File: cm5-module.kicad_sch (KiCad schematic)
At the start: 0 parts

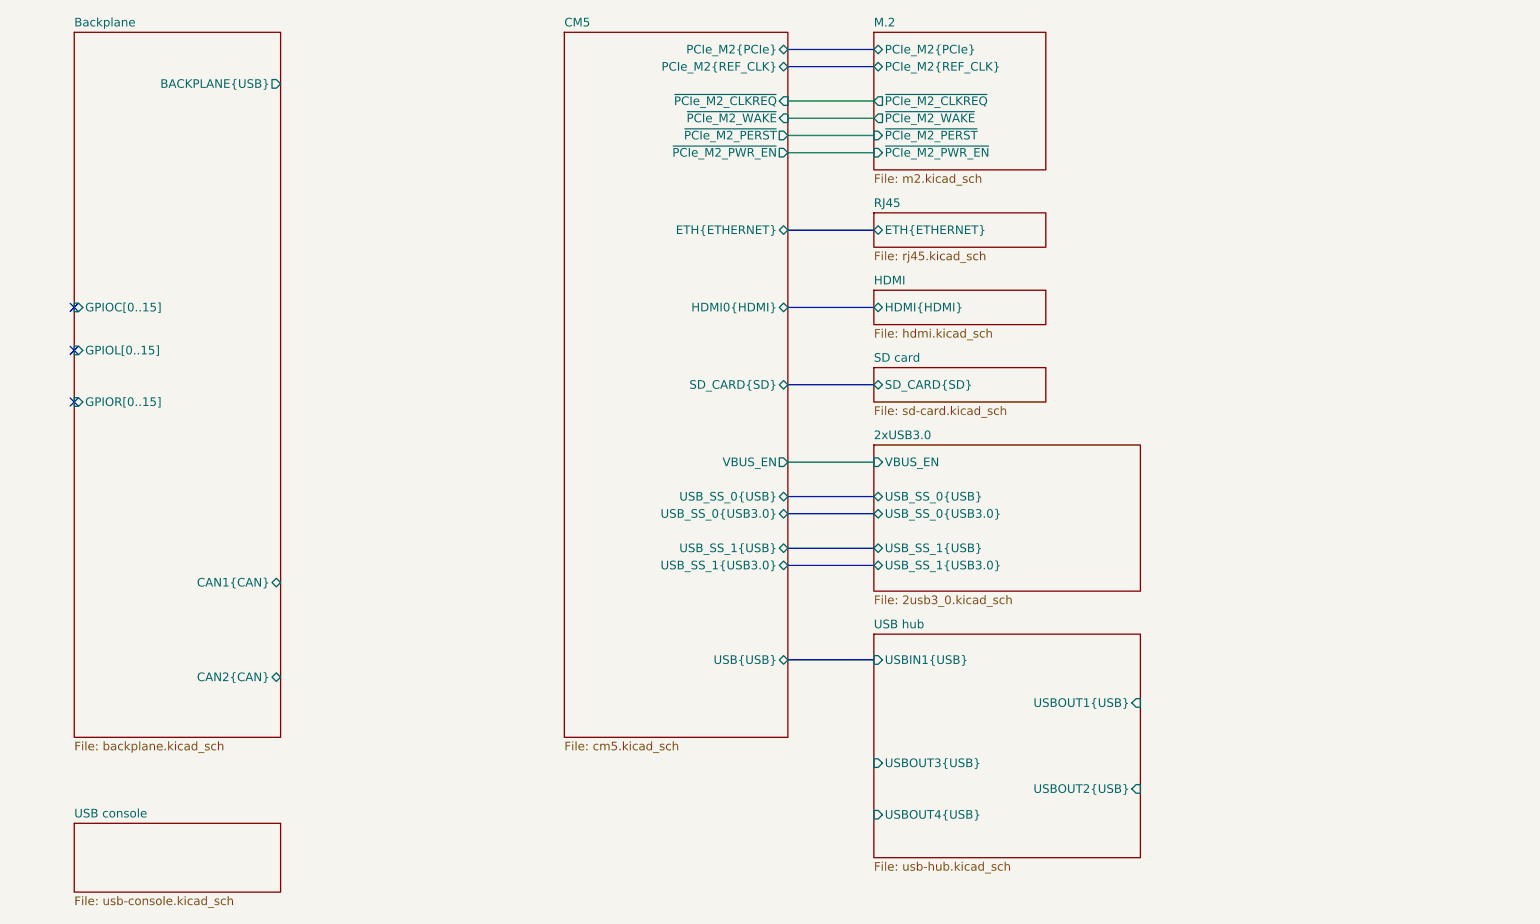
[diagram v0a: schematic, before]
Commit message: [#1] WIP: Change components to ones from the global library, refactor schematic
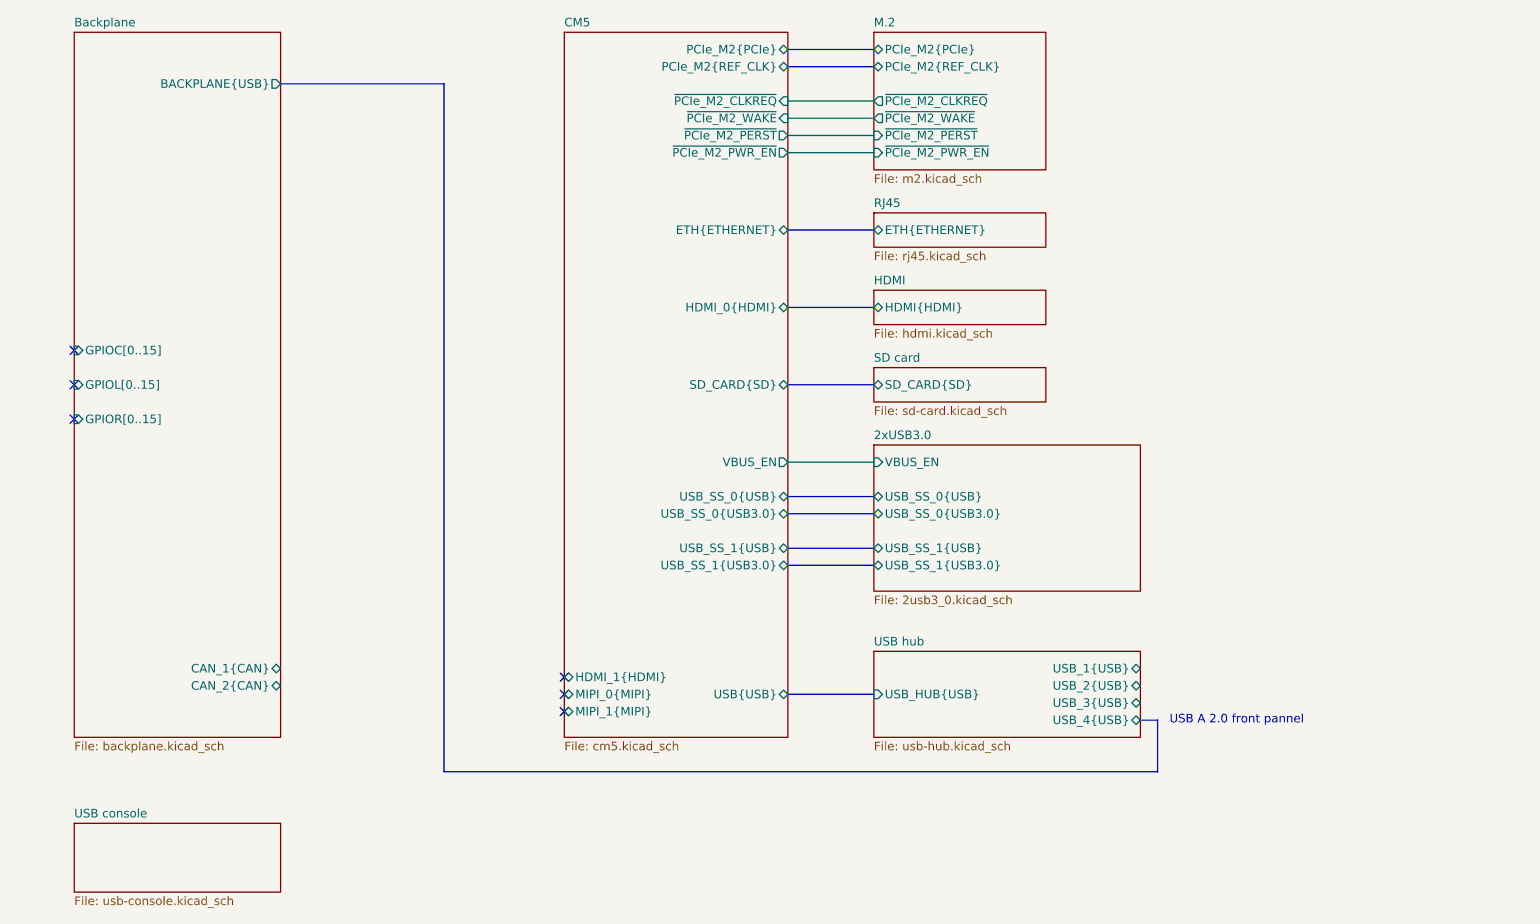
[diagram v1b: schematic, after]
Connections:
- no-connect marks 3 -> 6
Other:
- sheet Backplane ports: added CAN_1{CAN}, CAN_2{CAN}; removed CAN1{CAN}, CAN2{CAN}
- sheet CM5 ports: added HDMI_0{HDMI}, HDMI_1{HDMI}, MIPI_0{MIPI}, MIPI_1{MIPI}; removed HDMI0{HDMI}
- sheet USB hub ports: added USB_1{USB}, USB_2{USB}, USB_3{USB}, USB_4{USB}, USB_HUB{USB}; removed USBIN1{USB}, USBOUT1{USB}, USBOUT2{USB}, USBOUT3{USB}, USBOUT4{USB}
- note added: "USB A 2.0 front pannel"
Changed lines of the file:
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@@
 		(members "+" "-")
 	)
-	(no_connect
-		(at 46.99 78.74)
+	(text "USB A 2.0 front pannel"
+		(exclude_from_sim no)
+		(at 218.694 139.7 0)
+		(effects
+			(font
+				(size 1.27 1.27)
+			)
+		)
 	)
 	(no_connect
@@
 	)
 	(no_connect
-		(at 46.99 92.71)
+		(at 46.99 90.17)
+	)
+	(no_connect
+		(at 119.38 135.89)
+	)
+	(no_connect
+		(at 119.38 133.35)
+	)
+	(no_connect
+		(at 119.38 138.43)
+	)
+	(no_connect
+		(at 46.99 95.25)
 	)
 	(bus
@@
 	(bus
 		(pts
-			(xy 152.4 130.81) (xy 165.1 130.81)
+			(xy 152.4 135.89) (xy 165.1 135.89)
 		)
 		(stroke
@@
 	(bus
 		(pts
+			(xy 207.01 147.32) (xy 101.6 147.32)
+		)
+		(stroke
+			(width 0)
+			(type default)
+		)
+	)
+	(bus
+		(pts
+			(xy 101.6 147.32) (xy 101.6 45.72)
+		)
+		(stroke
+			(width 0)
+			(type default)
+		)
+	)
+	(bus
+		(pts
 			(xy 152.4 114.3) (xy 165.1 114.3)
 		)
@@
 		)
 	)
+	(bus
+		(pts
+			(xy 207.01 139.7) (xy 207.01 147.32)
+		)
+		(stroke
+			(width 0)
+			(type default)
+		)
+	)
 	(wire
 		(pts
@@
 		(pts
 			(xy 152.4 78.74) (xy 165.1 78.74)
+		)
+		(stroke
+			(width 0)
+			(type default)
+		)
+	)
+	(bus
+		(pts
+			(xy 204.47 139.7) (xy 207.01 139.7)
+		)
+		(stroke
+			(width 0)
+			(type default)
+		)
+	)
+	(bus
+		(pts
+			(xy 101.6 45.72) (xy 77.47 45.72)
 		)
 		(stroke
@@
 		)
 		(fill
-			(color 0 0 0 0.0000)
+			(color 255 255 194 1.0000)
 		)
 		(property "Sheetname" "USB console"
@@
 		)
 		(fill
-			(color 0 0 0 0.0000)
+			(color 255 255 194 1.0000)
 		)
 		(property "Sheetname" "M.2"
@@
 	)
 	(sheet
-		(at 165.1 127)
-		(size 39.37 33.02)
+		(at 165.1 129.54)
+		(size 39.37 12.7)
 		(exclude_from_sim no)
 		(in_bom yes)
@@
 		)
 		(fill
-			(color 0 0 0 0.0000)
+			(color 255 255 194 1.0000)
 		)
 		(property "Sheetname" "USB hub"
-			(at 165.1 126.2884 0)
+			(at 165.1 128.8284 0)
 			(effects
 				(font
@@
 		)
 		(property "Sheetfile" "usb-hub.kicad_sch"
-			(at 165.1 160.6046 0)
+			(at 165.1 142.8246 0)
 			(effects
 				(font
@@
 			)
 		)
-		(pin "USBIN1{USB}" input
-			(at 165.1 130.81 180)
-			(effects
-				(font
-					(size 1.27 1.27)
-				)
-				(justify left)
-			)
-		)
-		(pin "USBOUT3{USB}" input
-			(at 165.1 146.05 180)
-			(effects
-				(font
-					(size 1.27 1.27)
-				)
-				(justify left)
-			)
-		)
-		(pin "USBOUT2{USB}" input
-			(at 204.47 149.86 0)
-			(effects
-				(font
-					(size 1.27 1.27)
-				)
-				(justify right)
-			)
-		)
-		(pin "USBOUT4{USB}" input
-			(at 165.1 153.67 180)
-			(effects
-				(font
-					(size 1.27 1.27)
-				)
-				(justify left)
-			)
-		)
-		(pin "USBOUT1{USB}" input
+		(pin "USB_1{USB}" bidirectional
+			(at 204.47 132.08 0)
+			(effects
+				(font
+					(size 1.27 1.27)
+				)
+				(justify right)
+			)
+		)
+		(pin "USB_2{USB}" bidirectional
+			(at 204.47 134.62 0)
+			(effects
+				(font
+					(size 1.27 1.27)
+				)
+				(justify right)
+			)
+		)
+		(pin "USB_3{USB}" bidirectional
 			(at 204.47 137.16 0)
 			(effects
@@
 				)
 				(justify right)
+			)
+		)
+		(pin "USB_4{USB}" bidirectional
+			(at 204.47 139.7 0)
+			(effects
+				(font
+					(size 1.27 1.27)
+				)
+				(justify right)
+			)
+		)
+		(pin "USB_HUB{USB}" input
+			(at 165.1 135.89 180)
+			(effects
+				(font
+					(size 1.27 1.27)
+				)
+				(justify left)
 			)
 		)
@@
 		)
 		(fill
-			(color 0 0 0 0.0000)
+			(color 255 255 194 1.0000)
 		)
 		(property "Sheetname" "2xUSB3.0"
@@
 		)
 		(fill
-			(color 0 0 0 0.0000)
+			(color 255 255 194 1.0000)
 		)
 		(property "Sheetname" "HDMI"
@@
 		)
 		(fill
-			(color 0 0 0 0.0000)
+			(color 255 255 194 1.0000)
 		)
 		(property "Sheetname" "RJ45"
@@
 		)
 		(fill
-			(color 0 0 0 0.0000)
+			(color 255 255 194 1.0000)
 		)
 		(property "Sheetname" "SD card"
@@
 		)
 		(fill
-			(color 0 0 0 0.0000)
+			(color 255 255 194 1.0000)
 		)
 		(property "Sheetname" "CM5"
@@
 		)
 		(pin "USB{USB}" bidirectional
-			(at 152.4 130.81 0)
-			(effects
-				(font
-					(size 1.27 1.27)
-				)
-				(justify right)
-			)
-		)
-		(pin "HDMI0{HDMI}" bidirectional
-			(at 152.4 78.74 0)
+			(at 152.4 135.89 0)
 			(effects
 				(font
@@
 				)
 				(justify right)
+			)
+		)
+		(pin "HDMI_1{HDMI}" bidirectional
+			(at 119.38 133.35 180)
+			(effects
+				(font
+					(size 1.27 1.27)
+				)
+				(justify left)
+			)
+		)
+		(pin "HDMI_0{HDMI}" bidirectional
+			(at 152.4 78.74 0)
+			(effects
+				(font
+					(size 1.27 1.27)
+				)
+				(justify right)
+			)
+		)
+		(pin "MIPI_0{MIPI}" bidirectional
+			(at 119.38 135.89 180)
+			(effects
+				(font
+					(size 1.27 1.27)
+				)
+				(justify left)
+			)
+		)
+		(pin "MIPI_1{MIPI}" bidirectional
+			(at 119.38 138.43 180)
+			(effects
+				(font
+					(size 1.27 1.27)
+				)
+				(justify left)
 			)
 		)
@@
 		)
 		(fill
-			(color 0 0 0 0.0000)
+			(color 255 255 194 1.0000)
 		)
 		(property "Sheetname" "Backplane"
@@
 		)
 		(pin "GPIOC[0..15]" input
-			(at 46.99 78.74 180)
+			(at 46.99 85.09 180)
 			(effects
 				(font
@@
 		)
 		(pin "GPIOL[0..15]" input
-			(at 46.99 85.09 180)
+			(at 46.99 90.17 180)
 			(effects
 				(font
@@
 		)
 		(pin "GPIOR[0..15]" input
-			(at 46.99 92.71 180)
-			(effects
-				(font
-					(size 1.27 1.27)
-				)
-				(justify left)
-			)
-		)
-		(pin "CAN1{CAN}" bidirectional
-			(at 77.47 119.38 0)
-			(effects
-				(font
-					(size 1.27 1.27)
-				)
-				(justify right)
-			)
-		)
-		(pin "CAN2{CAN}" bidirectional
-			(at 77.47 133.35 0)
-			(effects
-				(font
-					(size 1.27 1.27)
-				)
-				(justify right)
+			(at 46.99 95.25 180)
+			(effects
+				(font
+					(size 1.27 1.27)
+				)
+				(justify left)
 			)
 		)
@@
 			(effects
 				(font
+					(size 1.27 1.27)
+				)
+				(justify right)
+			)
+		)
+		(pin "CAN_1{CAN}" bidirectional
+			(at 77.47 132.08 0)
+			(effects
+				(font
+					(size 1.27 1.27)
+				)
+				(justify right)
+			)
+		)
+		(pin "CAN_2{CAN}" bidirectional
+			(at 77.47 134.62 0)
+			(effects
+				(font

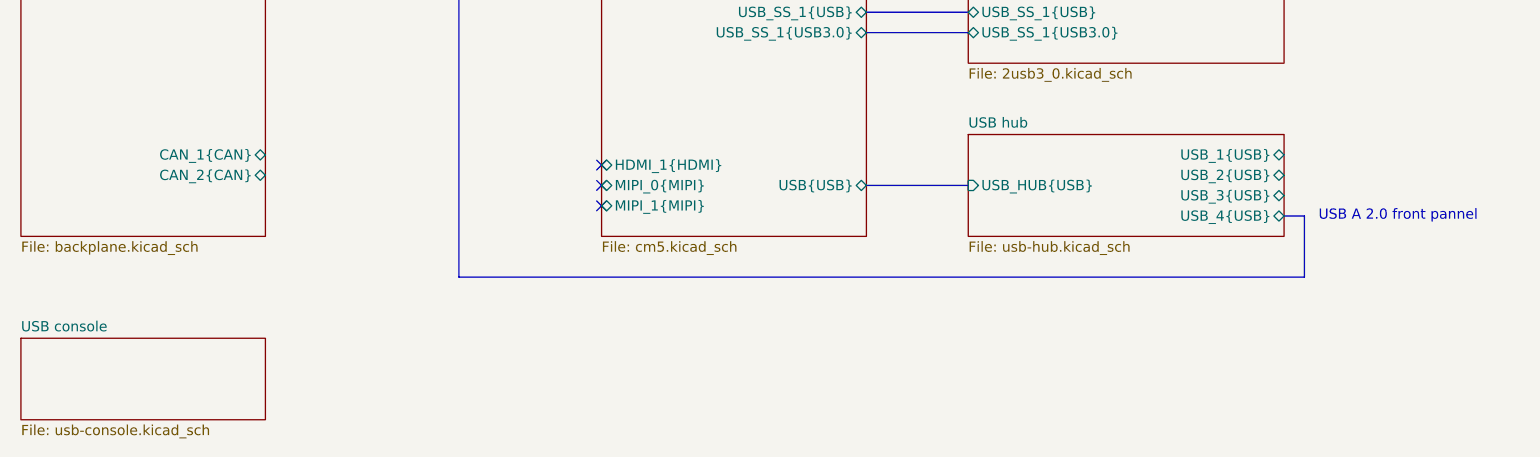
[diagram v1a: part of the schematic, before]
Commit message: [#1] Change components to ones from the global library, add debug console, refactor schematic
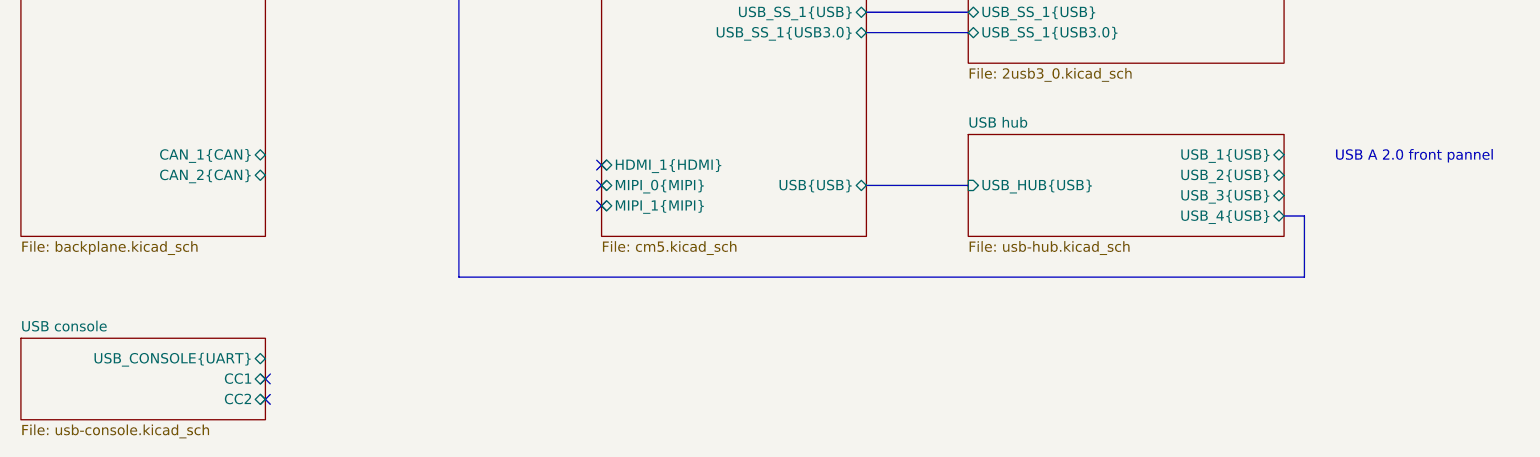
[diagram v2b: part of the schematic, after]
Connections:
- no-connect marks 6 -> 8
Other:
- sheet USB console ports: added CC1, CC2, USB_CONSOLE{UART}; removed none
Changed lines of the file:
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@@
 	(text "USB A 2.0 front pannel"
 		(exclude_from_sim no)
-		(at 218.694 139.7 0)
+		(at 220.726 132.334 0)
 		(effects
 			(font
@@
 	)
 	(no_connect
+		(at 77.47 162.56)
+	)
+	(no_connect
 		(at 46.99 90.17)
 	)
 	(no_connect
 		(at 119.38 135.89)
+	)
+	(no_connect
+		(at 77.47 160.02)
 	)
 	(no_connect
@@
 			)
 		)
+		(pin "USB_CONSOLE{UART}" bidirectional
+			(at 77.47 157.48 0)
+			(effects
+				(font
+					(size 1.27 1.27)
+				)
+				(justify right)
+			)
+		)
+		(pin "CC1" bidirectional
+			(at 77.47 160.02 0)
+			(effects
+				(font
+					(size 1.27 1.27)
+				)
+				(justify right)
+			)
+		)
+		(pin "CC2" bidirectional
+			(at 77.47 162.56 0)
+			(effects
+				(font
+					(size 1.27 1.27)
+				)
+				(justify right)
+			)
+		)

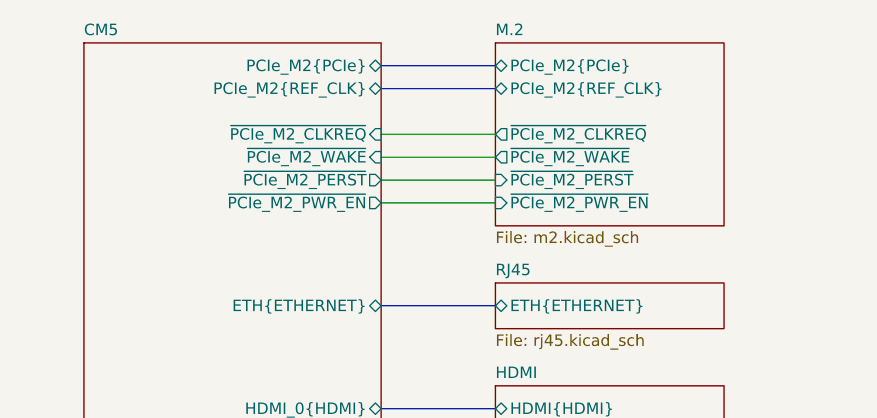
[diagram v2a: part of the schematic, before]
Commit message: [#1] Add bus colors, rename PCIe signals
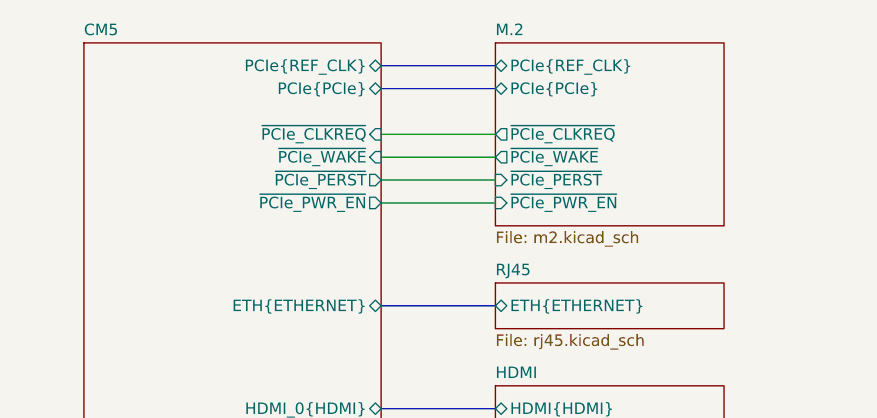
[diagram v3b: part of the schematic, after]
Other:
- sheet CM5 ports: added PCIe{PCIe}, PCIe{REF_CLK}, ~{PCIe_CLKREQ}, ~{PCIe_PERST}, ~{PCIe_PWR_EN}, ~{PCIe_WAKE}; removed PCIe_M2{PCIe}, PCIe_M2{REF_CLK}, ~{PCIe_M2_CLKREQ}, ~{PCIe_M2_PERST}, ~{PCIe_M2_PWR_EN}, ~{PCIe_M2_WAKE}
- sheet M.2 ports: added PCIe{PCIe}, PCIe{REF_CLK}, ~{PCIe_CLKREQ}, ~{PCIe_PERST}, ~{PCIe_PWR_EN}, ~{PCIe_WAKE}; removed PCIe_M2{PCIe}, PCIe_M2{REF_CLK}, ~{PCIe_M2_CLKREQ}, ~{PCIe_M2_PERST}, ~{PCIe_M2_PWR_EN}, ~{PCIe_M2_WAKE}
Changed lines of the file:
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@@
 			)
 		)
-		(pin "PCIe_M2{PCIe}" bidirectional
+		(pin "~{PCIe_CLKREQ}" output
+			(at 165.1 48.26 180)
+			(effects
+				(font
+					(size 1.27 1.27)
+				)
+				(justify left)
+			)
+		)
+		(pin "~{PCIe_PERST}" input
+			(at 165.1 53.34 180)
+			(effects
+				(font
+					(size 1.27 1.27)
+				)
+				(justify left)
+			)
+		)
+		(pin "~{PCIe_PWR_EN}" input
+			(at 165.1 55.88 180)
+			(effects
+				(font
+					(size 1.27 1.27)
+				)
+				(justify left)
+			)
+		)
+		(pin "~{PCIe_WAKE}" output
+			(at 165.1 50.8 180)
+			(effects
+				(font
+					(size 1.27 1.27)
+				)
+				(justify left)
+			)
+		)
+		(pin "PCIe{PCIe}" bidirectional
+			(at 165.1 43.18 180)
+			(effects
+				(font
+					(size 1.27 1.27)
+				)
+				(justify left)
+			)
+		)
+		(pin "PCIe{REF_CLK}" bidirectional
 			(at 165.1 40.64 180)
-			(effects
-				(font
-					(size 1.27 1.27)
-				)
-				(justify left)
-			)
-		)
-		(pin "PCIe_M2{REF_CLK}" bidirectional
-			(at 165.1 43.18 180)
-			(effects
-				(font
-					(size 1.27 1.27)
-				)
-				(justify left)
-			)
-		)
-		(pin "~{PCIe_M2_CLKREQ}" output
-			(at 165.1 48.26 180)
-			(effects
-				(font
-					(size 1.27 1.27)
-				)
-				(justify left)
-			)
-		)
-		(pin "~{PCIe_M2_PERST}" input
-			(at 165.1 53.34 180)
-			(effects
-				(font
-					(size 1.27 1.27)
-				)
-				(justify left)
-			)
-		)
-		(pin "~{PCIe_M2_PWR_EN}" input
-			(at 165.1 55.88 180)
-			(effects
-				(font
-					(size 1.27 1.27)
-				)
-				(justify left)
-			)
-		)
-		(pin "~{PCIe_M2_WAKE}" output
-			(at 165.1 50.8 180)
 			(effects
 				(font
@@
 			)
 		)
-		(pin "PCIe_M2{REF_CLK}" bidirectional
-			(at 152.4 43.18 0)
-			(effects
-				(font
-					(size 1.27 1.27)
-				)
-				(justify right)
-			)
-		)
-		(pin "PCIe_M2{PCIe}" bidirectional
-			(at 152.4 40.64 0)
-			(effects
-				(font
-					(size 1.27 1.27)
-				)
-				(justify right)
-			)
-		)
-		(pin "~{PCIe_M2_CLKREQ}" input
-			(at 152.4 48.26 0)
-			(effects
-				(font
-					(size 1.27 1.27)
-				)
-				(justify right)
-			)
-		)
-		(pin "~{PCIe_M2_PWR_EN}" output
-			(at 152.4 55.88 0)
-			(effects
-				(font
-					(size 1.27 1.27)
-				)
-				(justify right)
-			)
-		)
-		(pin "~{PCIe_M2_WAKE}" input
-			(at 152.4 50.8 0)
-			(effects
-				(font
-					(size 1.27 1.27)
-				)
-				(justify right)
-			)
-		)
-		(pin "~{PCIe_M2_PERST}" output
-			(at 152.4 53.34 0)
-			(effects
-				(font
-					(size 1.27 1.27)
-				)
-				(justify right)
-			)
-		)
 		(pin "USB{USB}" bidirectional
 			(at 152.4 135.89 0)
@@
 			)
 		)
+		(pin "PCIe{PCIe}" bidirectional
+			(at 152.4 43.18 0)
+			(effects
+				(font
+					(size 1.27 1.27)
+				)
+				(justify right)
+			)
+		)
+		(pin "PCIe{REF_CLK}" bidirectional
+			(at 152.4 40.64 0)
+			(effects
+				(font
+					(size 1.27 1.27)
+				)
+				(justify right)
+			)
+		)
+		(pin "~{PCIe_CLKREQ}" input
+			(at 152.4 48.26 0)
+			(effects
+				(font
+					(size 1.27 1.27)
+				)
+				(justify right)
+			)
+		)
+		(pin "~{PCIe_PERST}" output
+			(at 152.4 53.34 0)
+			(effects
+				(font
+					(size 1.27 1.27)
+				)
+				(justify right)
+			)
+		)
+		(pin "~{PCIe_PWR_EN}" output
+			(at 152.4 55.88 0)
+			(effects
+				(font
+					(size 1.27 1.27)
+				)
+				(justify right)
+			)
+		)
+		(pin "~{PCIe_WAKE}" input
+			(at 152.4 50.8 0)
+			(effects
+				(font
+					(size 1.27 1.27)
+				)
+				(justify right)
+			)
+		)
